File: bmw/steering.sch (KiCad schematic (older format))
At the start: 16 parts, among them P1 CONN_01X03, P2 CONN_01X12, P3 CONN_01X03, P4 CONN_01X12, U1 ProMicro, U2 TH3122, U3 MCP41100, U4 4053

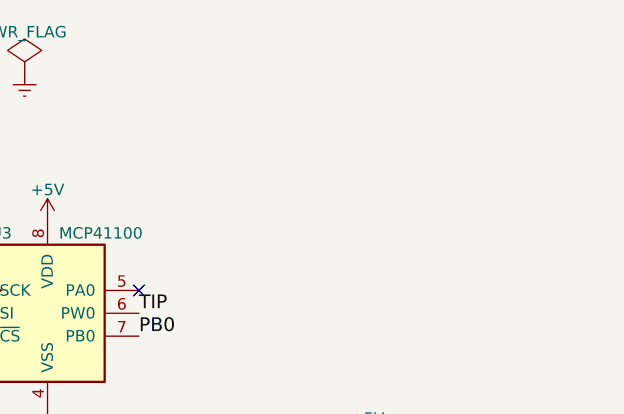
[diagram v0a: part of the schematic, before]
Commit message: Zrezygnowano z przetwornicy na rzecz LDO LM1117 5V. Pozostało połączyć masę układu w dwóch punktach. Poprawnie przechodzi testy DRC. Można wykonać prototyp.
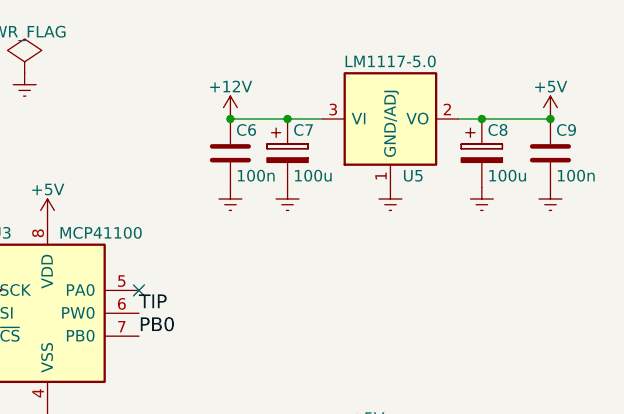
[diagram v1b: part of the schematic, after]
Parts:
- added C6, C9: 100n, Capacitors_SMD:C_0603_HandSoldering, symbol C
- added C7, C8: 100u, Capacitors_SMD:c_elec_10x10, symbol CP
- added U5: LM1117-5.0, TO_SOT_Packages_SMD:SOT-223, symbol LM1117-5.0
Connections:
- net +12V: now also C6.1, C7.1, U5.3 (VI)
- net +5V: now also C8.1, C9.1, U5.2 (VO), U5.4 (VO)
- net Earth: now also C6.2, C7.2, C8.2, C9.2, U5.1 (GND/ADJ)
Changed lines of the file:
@@
 LIBS:valves
 LIBS:microchip_pot
-LIBS:warsztaty
 LIBS:steering-cache
 EELAYER 25 0
@@
 $EndComp
 $Comp
-L +12V #PWR?
+L +12V #PWR025
 U 1 1 58A5F05B
 P 1400 3650
-F 0 "#PWR?" H 1400 3500 50  0001 C CNN
+F 0 "#PWR025" H 1400 3500 50  0001 C CNN
 F 1 "+12V" H 1400 3790 50  0000 C CNN
 F 2 "" H 1400 3650 60  0000 C CNN
@@
 	1    0    0    -1
 $EndComp
+$Comp
+L LM1117-5.0 U5
+U 1 1 58EA39AB
+P 6050 1200
+F 0 "U5" H 6150 950 50  0000 C CNN
+F 1 "LM1117-5.0" H 6050 1450 50  0000 C CNN
+F 2 "TO_SOT_Packages_SMD:SOT-223" H 6050 1200 50  0001 C CNN
+F 3 "" H 6050 1200 50  0000 C CNN
+	1    6050 1200
+	1    0    0    -1
+$EndComp
+$Comp
+L Earth #PWR026
+U 1 1 58EA3C7F
+P 6050 1500
+F 0 "#PWR026" H 6050 1250 50  0001 C CNN
+F 1 "Earth" H 6050 1350 50  0001 C CNN
+F 2 "" H 6050 1500 60  0000 C CNN
+F 3 "" H 6050 1500 60  0000 C CNN
+	1    6050 1500
+	1    0    0    -1
+$EndComp
+$Comp
+L +12V #PWR027
+U 1 1 58EA3D89
+P 5350 1200
+F 0 "#PWR027" H 5350 1050 50  0001 C CNN
+F 1 "+12V" H 5350 1340 50  0000 C CNN
+F 2 "" H 5350 1200 60  0000 C CNN
+F 3 "" H 5350 1200 60  0000 C CNN
+	1    5350 1200
+	1    0    0    -1
+$EndComp
+$Comp
+L +5V #PWR028
+U 1 1 58EA3E0B
+P 6750 1200
+F 0 "#PWR028" H 6750 1050 50  0001 C CNN
+F 1 "+5V" H 6750 1340 50  0000 C CNN
+F 2 "" H 6750 1200 60  0000 C CNN
+F 3 "" H 6750 1200 60  0000 C CNN
+	1    6750 1200
+	1    0    0    -1
+$EndComp
+$Comp
+L CP C7
+U 1 1 58EA3EE2
+P 5600 1350
+F 0 "C7" H 5625 1450 50  0000 L CNN
+F 1 "100u" H 5625 1250 50  0000 L CNN
+F 2 "Capacitors_SMD:c_elec_10x10" H 5638 1200 30  0001 C CNN
+F 3 "" H 5600 1350 60  0000 C CNN
+	1    5600 1350
+	1    0    0    -1
+$EndComp
+$Comp
+L CP C8
+U 1 1 58EA40D8
+P 6450 1350
+F 0 "C8" H 6475 1450 50  0000 L CNN
+F 1 "100u" H 6475 1250 50  0000 L CNN
+F 2 "Capacitors_SMD:c_elec_10x10" H 6488 1200 30  0001 C CNN
+F 3 "" H 6450 1350 60  0000 C CNN
+	1    6450 1350
+	1    0    0    -1
+$EndComp
+$Comp
+L Earth #PWR029
+U 1 1 58EA4159
+P 5350 1500
+F 0 "#PWR029" H 5350 1250 50  0001 C CNN
+F 1 "Earth" H 5350 1350 50  0001 C CNN
+F 2 "" H 5350 1500 60  0000 C CNN
+F 3 "" H 5350 1500 60  0000 C CNN
+	1    5350 1500
+	1    0    0    -1
+$EndComp
+$Comp
+L Earth #PWR030
+U 1 1 58EA419D
+P 6450 1500
+F 0 "#PWR030" H 6450 1250 50  0001 C CNN
+F 1 "Earth" H 6450 1350 50  0001 C CNN
+F 2 "" H 6450 1500 60  0000 C CNN
+F 3 "" H 6450 1500 60  0000 C CNN
+	1    6450 1500
+	1    0    0    -1
+$EndComp
+$Comp
+L C C6
+U 1 1 58EA42B2
+P 5350 1350
+F 0 "C6" H 5375 1450 50  0000 L CNN
+F 1 "100n" H 5375 1250 50  0000 L CNN
+F 2 "Capacitors_SMD:C_0603_HandSoldering" H 5388 1200 30  0001 C CNN
+F 3 "" H 5350 1350 60  0000 C CNN
+	1    5350 1350
+	1    0    0    -1
+$EndComp
+$Comp
+L C C9
+U 1 1 58EA441C
+P 6750 1350
+F 0 "C9" H 6775 1450 50  0000 L CNN
+F 1 "100n" H 6775 1250 50  0000 L CNN
+F 2 "Capacitors_SMD:C_0603_HandSoldering" H 6788 1200 30  0001 C CNN
+F 3 "" H 6750 1350 60  0000 C CNN
+	1    6750 1350
+	1    0    0    -1
+$EndComp
+Wire Wire Line
+	5350 1200 5750 1200
+Connection ~ 5600 1200
+Connection ~ 5350 1200
+Wire Wire Line
+	6350 1200 6750 1200
+Connection ~ 6450 1200
+Connection ~ 6750 1200
+$Comp
+L Earth #PWR031
+U 1 1 58EA476B
+P 5600 1500
+F 0 "#PWR031" H 5600 1250 50  0001 C CNN
+F 1 "Earth" H 5600 1350 50  0001 C CNN
+F 2 "" H 5600 1500 60  0000 C CNN
+F 3 "" H 5600 1500 60  0000 C CNN
+	1    5600 1500
+	1    0    0    -1
+$EndComp
+$Comp
+L Earth #PWR032
+U 1 1 58EA47B5
+P 6750 1500
+F 0 "#PWR032" H 6750 1250 50  0001 C CNN
+F 1 "Earth" H 6750 1350 50  0001 C CNN
+F 2 "" H 6750 1500 60  0000 C CNN
+F 3 "" H 6750 1500 60  0000 C CNN
+	1    6750 1500
+	1    0    0    -1
+$EndComp
